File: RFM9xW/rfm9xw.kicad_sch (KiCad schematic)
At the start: 9 parts, among them J1 Conn1, J2 Conn2, J3 U.FL / IPEX, J4 SMA, U1 RFM9x

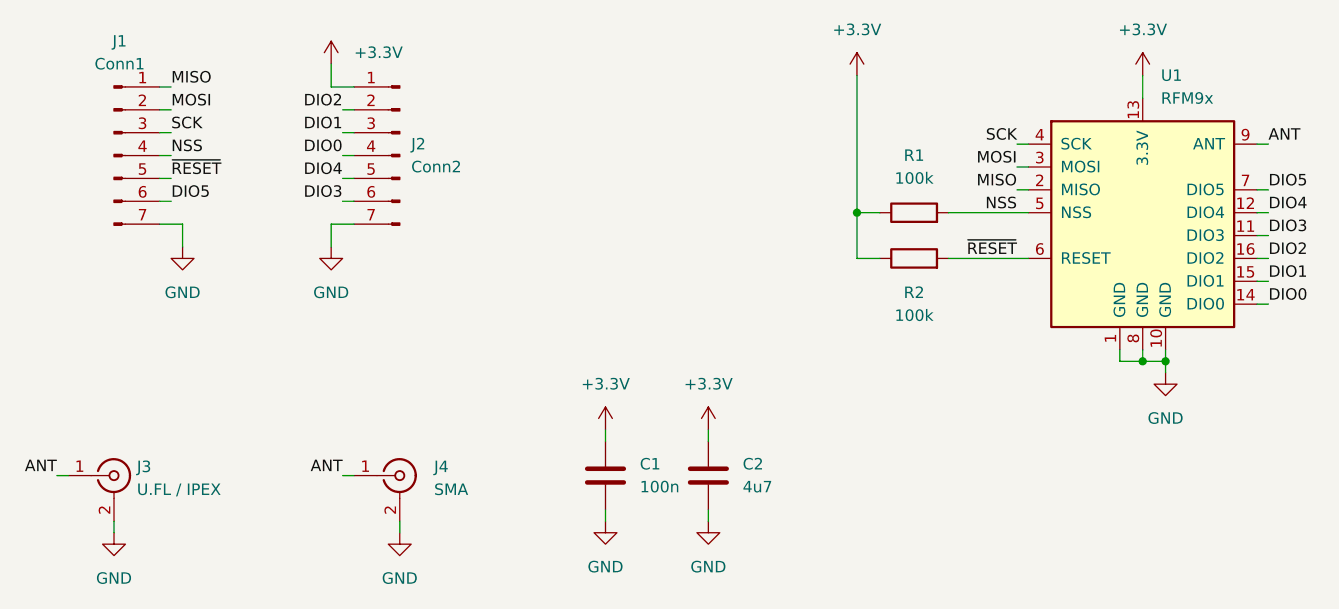
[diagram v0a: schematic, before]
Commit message: Updated the RFM69W and RFM95W/RFM96W board layouts.
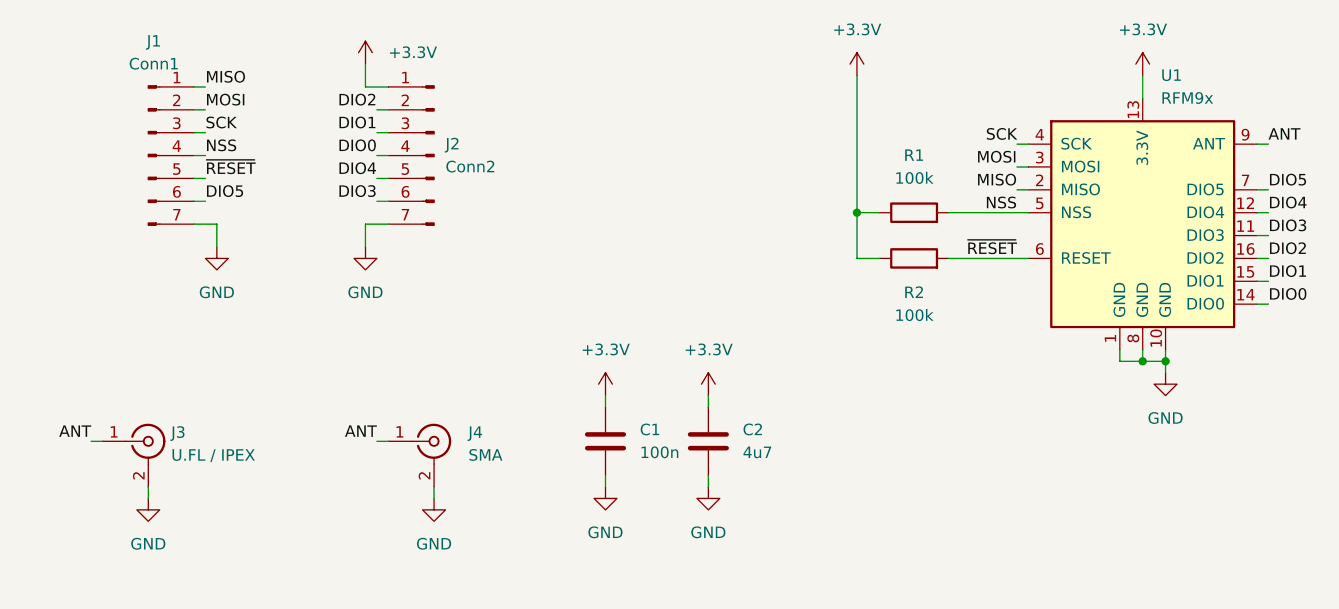
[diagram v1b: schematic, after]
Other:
- moved on the sheet: C1, C2, J1, J2, J3, J4
